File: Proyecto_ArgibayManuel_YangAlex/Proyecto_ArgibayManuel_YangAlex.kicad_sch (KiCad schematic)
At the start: 27 parts, among them J2 Conn_01x04, J3 Conn_01x06, J4 Conn_01x05, SW1 SW_Push, SW2 SW_Push, SW3 SW_Push, SW4 SW_Push, U1 PIC18F258-I_SO, U2 LT1716IS5TRMPBF, U3 LT1716IS5TRMPBF, U7 HDC2010YPAR, U8 TXS0108EPW, Y1 Crystal

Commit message: icsp
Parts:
- added J5: Conn_01x03_Pin, symbol Connector:Conn_01x03_Pin
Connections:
- net F_C_Out1: now also U1.17 (RC6/TX/CK); no longer U1.25 (RB4)
- net F_C_Out2: now also U1.18 (RC7/RX/DT); no longer U1.26 (RB5/PGM)
- net MCLR: now also J5.2 (Pin_2); no longer R3.1, SW4.1
- net PGC: now reaches U1.27 (RB6/PGC)
- net PGD: now reaches U1.28 (RB7/PGD)
- net +12V renamed VBat
- new net: J5.1 (Pin_1), R3.1, SW4.1
- new net PGM: U1.26 (RB5/PGM)
- new net Vpp: J5.3 (Pin_3)
- no-connect marks 26 -> 23
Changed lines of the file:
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@@
 	)
 	(junction
-		(at 33.02 27.94)
-		(diameter 0)
-		(color 0 0 0 0)
-	)
-	(junction
 		(at 250.19 39.37)
 		(diameter 0)
@@
 	)
 	(junction
-		(at 152.4 170.18)
+		(at 157.48 170.18)
 		(diameter 0)
 		(color 0 0 0 0)
@@
 	)
 	(no_connect
-		(at 110.49 125.73)
-	)
-	(no_connect
 		(at 247.65 59.69)
 	)
@@
 	)
 	(no_connect
-		(at 267.97 57.15)
+		(at 110.49 134.62)
 	)
 	(no_connect
-		(at 110.49 166.37)
+		(at 267.97 57.15)
 	)
 	(no_connect
@@
 	)
 	(no_connect
-		(at 110.49 129.54)
-	)
-	(no_connect
 		(at 267.97 54.61)
 	)
 	(no_connect
-		(at 110.49 163.83)
-	)
-	(no_connect
 		(at 267.97 67.31)
 	)
@@
 	(wire
 		(pts
-			(xy 30.48 27.94) (xy 33.02 27.94)
-		)
-		(stroke
-			(width 0)
-			(type default)
-		)
-	)
-	(wire
-		(pts
 			(xy 205.74 151.13) (xy 213.36 151.13)
 		)
@@
 	(wire
 		(pts
-			(xy 152.4 170.18) (xy 158.75 170.18)
+			(xy 152.4 170.18) (xy 157.48 170.18)
 		)
 		(stroke
@@
 	(wire
 		(pts
-			(xy 66.04 45.72) (xy 67.31 45.72)
+			(xy 157.48 170.18) (xy 157.48 180.34)
 		)
 		(stroke
@@
 	(wire
 		(pts
-			(xy 99.06 109.22) (xy 99.06 110.49)
+			(xy 66.04 45.72) (xy 67.31 45.72)
 		)
 		(stroke
@@
 	(wire
 		(pts
-			(xy 149.86 170.18) (xy 152.4 170.18)
+			(xy 99.06 109.22) (xy 99.06 110.49)
 		)
 		(stroke
@@
 	(wire
 		(pts
-			(xy 33.02 27.94) (xy 33.02 35.56)
-		)
-		(stroke
-			(width 0)
-			(type default)
-		)
-	)
-	(wire
-		(pts
 			(xy 250.19 39.37) (xy 250.19 43.18)
 		)
@@
 	(wire
 		(pts
-			(xy 33.02 26.67) (xy 33.02 27.94)
+			(xy 33.02 25.4) (xy 33.02 35.56)
 		)
 		(stroke
@@
 	(wire
 		(pts
+			(xy 157.48 180.34) (xy 152.4 180.34)
+		)
+		(stroke
+			(width 0)
+			(type default)
+		)
+	)
+	(wire
+		(pts
 			(xy 87.63 194.31) (xy 91.44 194.31)
 		)
@@
 	(wire
 		(pts
+			(xy 157.48 170.18) (xy 158.75 170.18)
+		)
+		(stroke
+			(width 0)
+			(type default)
+		)
+	)
+	(wire
+		(pts
 			(xy 238.76 39.37) (xy 240.03 39.37)
 		)
@@
 	(wire
 		(pts
+			(xy 152.4 182.88) (xy 157.48 182.88)
+		)
+		(stroke
+			(width 0)
+			(type default)
+		)
+	)
+	(wire
+		(pts
 			(xy 25.4 128.27) (xy 27.94 128.27)
 		)
@@
 	(wire
 		(pts
+			(xy 152.4 185.42) (xy 154.94 185.42)
+		)
+		(stroke
+			(width 0)
+			(type default)
+		)
+	)
+	(wire
+		(pts
 			(xy 48.26 35.56) (xy 41.91 35.56)
 		)
@@
 	(global_label "VBat"
 		(shape input)
-		(at 30.48 27.94 180)
+		(at 33.02 25.4 0)
 		(fields_autoplaced yes)
 		(effects
@@
 				(size 1.27 1.27)
 			)
-			(justify right)
+			(justify left)
 		)
 		(property "Intersheetrefs" "${INTERSHEET_REFS}"
-			(at 23.2615 27.94 0)
+			(at 40.2385 25.4 0)
 			(effects
 				(font
 					(size 1.27 1.27)
 				)
-				(justify right)
+				(justify left)
 				(hide yes)
 			)
@@
 	(global_label "F_C_Out2"
 		(shape input)
-		(at 110.49 132.08 0)
+		(at 110.49 163.83 0)
 		(fields_autoplaced yes)
 		(effects
@@
 		)
 		(property "Intersheetrefs" "${INTERSHEET_REFS}"
-			(at 122.1837 132.08 0)
+			(at 122.1837 163.83 0)
 			(effects
 				(font
@@
 	(global_label "MCLR"
 		(shape input)
-		(at 149.86 170.18 180)
+		(at 157.48 182.88 0)
 		(fields_autoplaced yes)
 		(effects
@@
 				(size 1.27 1.27)
 			)
-			(justify right)
+			(justify left)
 		)
 		(property "Intersheetrefs" "${INTERSHEET_REFS}"
-			(at 141.8553 170.18 0)
+			(at 165.4847 182.88 0)
 			(effects
 				(font
 					(size 1.27 1.27)
 				)
-				(justify right)
+				(justify left)
 				(hide yes)
 			)
@@
 		)
 	)
+	(global_label "PGM"
+		(shape input)
+		(at 110.49 132.08 0)
+		(fields_autoplaced yes)
+		(effects
+			(font
+				(size 1.27 1.27)
+			)
+			(justify left)
+		)
+		(property "Intersheetrefs" "${INTERSHEET_REFS}"
+			(at 117.4666 132.08 0)
+			(effects
+				(font
+					(size 1.27 1.27)
+				)
+				(justify left)
+				(hide yes)
+			)
+		)
+	)
 	(global_label "F_C_Out1"
 		(shape input)
-		(at 110.49 134.62 0)
+		(at 110.49 166.37 0)
 		(fields_autoplaced yes)
 		(effects
@@
 		)
 		(property "Intersheetrefs" "${INTERSHEET_REFS}"
-			(at 122.1837 134.62 0)
+			(at 122.1837 166.37 0)
 			(effects
 				(font
@@
 		)
 	)
+	(global_label "Vpp"
+		(shape input)
+		(at 154.94 185.42 0)
+		(fields_autoplaced yes)
+		(effects
+			(font
+				(size 1.27 1.27)
+			)
+			(justify left)
+		)
+		(property "Intersheetrefs" "${INTERSHEET_REFS}"
+			(at 161.3118 185.42 0)
+			(effects
+				(font
+					(size 1.27 1.27)
+				)
+				(justify left)
+				(hide yes)
+			)
+		)
+	)
+	(global_label "PGC"
+		(shape input)
+		(at 110.49 129.54 0)
+		(fields_autoplaced yes)
+		(effects
+			(font
+				(size 1.27 1.27)
+			)
+			(justify left)
+		)
+		(property "Intersheetrefs" "${INTERSHEET_REFS}"
+			(at 117.2852 129.54 0)
+			(effects
+				(font
+					(size 1.27 1.27)
+				)
+				(justify left)
+				(hide yes)
+			)
+		)
+	)
 	(global_label "C_R_Calefactor"
 		(shape input)
@@
 		)
 	)
+	(global_label "PGD"
+		(shape input)
+		(at 110.49 125.73 0)
+		(fields_autoplaced yes)
+		(effects
+			(font
+				(size 1.27 1.27)
+			)
+			(justify left)
+		)
+		(property "Intersheetrefs" "${INTERSHEET_REFS}"
+			(at 117.2852 125.73 0)
+			(effects
+				(font
+					(size 1.27 1.27)
+				)
+				(justify left)
+				(hide yes)
+			)
+		)
+	)
 	(global_label "TX1"
 		(shape input)
@@
 	)
 	(symbol
+		(lib_id "Connector:Conn_01x03_Pin")
+		(at 147.32 182.88 0)
+		(unit 1)
+		(exclude_from_sim no)
+		(in_bom yes)
+		(on_board yes)
+		(dnp no)
+		(fields_autoplaced yes)
+		(property "Reference" "J5"
+			(at 147.955 175.26 0)
+			(effects
+				(font
+					(size 1.27 1.27)
+				)
+			)
+		)
+		(property "Value" "Conn_01x03_Pin"
+			(at 147.955 177.8 0)
+			(effects
+				(font
+					(size 1.27 1.27)
+				)
+			)
+		)
+		(property "Footprint" ""
+			(at 147.32 182.88 0)
+			(effects
+				(font
+					(size 1.27 1.27)
+				)
+				(hide yes)
+			)
+		)
+		(property "Datasheet" "~"
+			(at 147.32 182.88 0)
+			(effects
+				(font
+					(size 1.27 1.27)
+				)
+				(hide yes)
+			)
+		)
+		(property "Description" "Generic connector, single row, 01x03, script generated"
+			(at 147.32 182.88 0)
+			(effects
+				(font
+					(size 1.27 1.27)
+				)
+				(hide yes)
+			)
+		)
+		(pin "3"
+		)
+		(pin "1"
+		)
+		(pin "2"
+		)
+		(instances
+			(project ""
+				(path "/b2dde924-33f5-41ab-a1bf-811873450a89"
+					(reference "J5")
+					(unit 1)
+				)
+			)
+		)
+	)
+	(symbol
 		(lib_id "Device:R")
 		(at 217.17 151.13 270)
@@
 					(unit 1)
 				)
-			)
-		)
-	)
-	(symbol
-		(lib_id "power:+12V")
-		(at 33.02 26.67 0)
-		(unit 1)
-		(exclude_from_sim no)
-		(in_bom yes)
-		(on_board yes)
-		(dnp no)
-		(property "Reference" "#PWR02"
-			(at 33.02 30.48 0)
-			(effects
-				(font
-					(size 1.27 1.27)
-				)
-				(hide yes)
-			)
-		)
-		(property "Value" "+12V"
-			(at 36.322 24.13 0)
-			(effects
-				(font
-					(size 1.27 1.27)
-				)
-			)
-		)
-		(property "Footprint" ""
-			(at 33.02 26.67 0)
-			(effects
-				(font
-					(size 1.27 1.27)
-				)
-				(hide yes)
-			)
-		)
-		(property "Datasheet" ""
-			(at 33.02 26.67 0)
-			(effects
-				(font
-					(size 1.27 1.27)
-				)
-				(hide yes)
-			)
-		)
-		(property "Description" "Power symbol creates a global label with name \"+12V\""
-			(at 33.02 26.67 0)
-			(effects
-				(font
-					(size 1.27 1.27)
-				)
-				(hide yes)
-			)
-		)
-		(pin "1"
-		)
-		(instances
-			(project ""
-				(path "/b2dde924-33f5-41ab-a1bf-811873450a89"
-					(reference "#PWR02")
-					(unit 1)
-				)

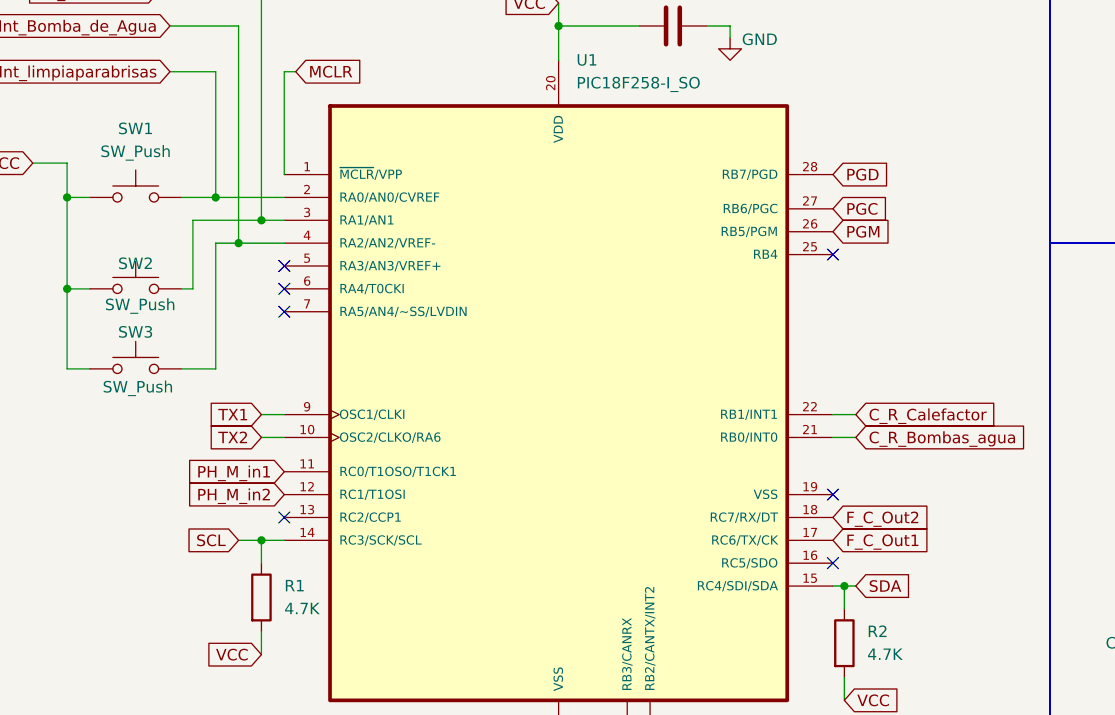
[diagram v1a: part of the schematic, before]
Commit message: Arreglo net classes, agrego DB-9
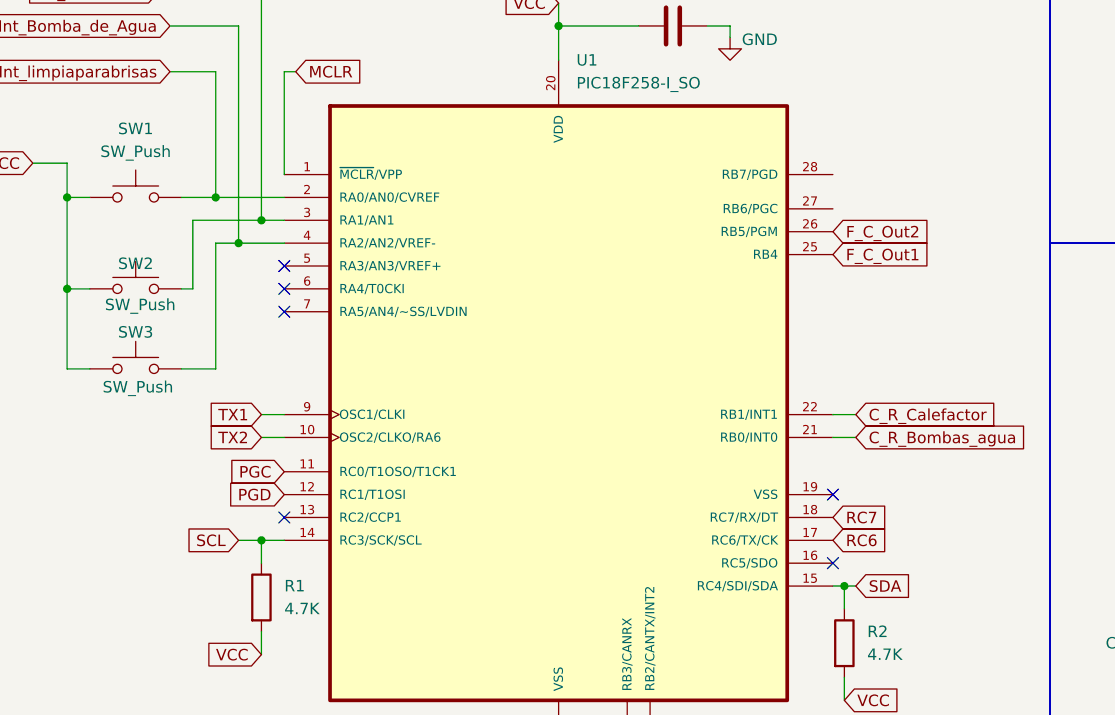
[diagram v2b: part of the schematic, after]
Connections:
- net PGM is gone; now on net F_C_Out2: U1.26 (RB5/PGM)
- net PH_M_in1 is gone; now on net PGC: U1.11 (RC0/T1OSO/T1CK1)
- net PH_M_in2 is gone; now on net PGD: U1.12 (RC1/T1OSI)
- net F_C_Out1: now also U1.25 (RB4); no longer U1.17 (RC6/TX/CK)
- net F_C_Out2: no longer U1.18 (RC7/RX/DT)
- net PGC: no longer U1.27 (RB6/PGC)
- net PGD: no longer U1.28 (RB7/PGD)
- new net RC6: U1.17 (RC6/TX/CK)
- new net RC7: U1.18 (RC7/RX/DT)
- no-connect marks 23 -> 22

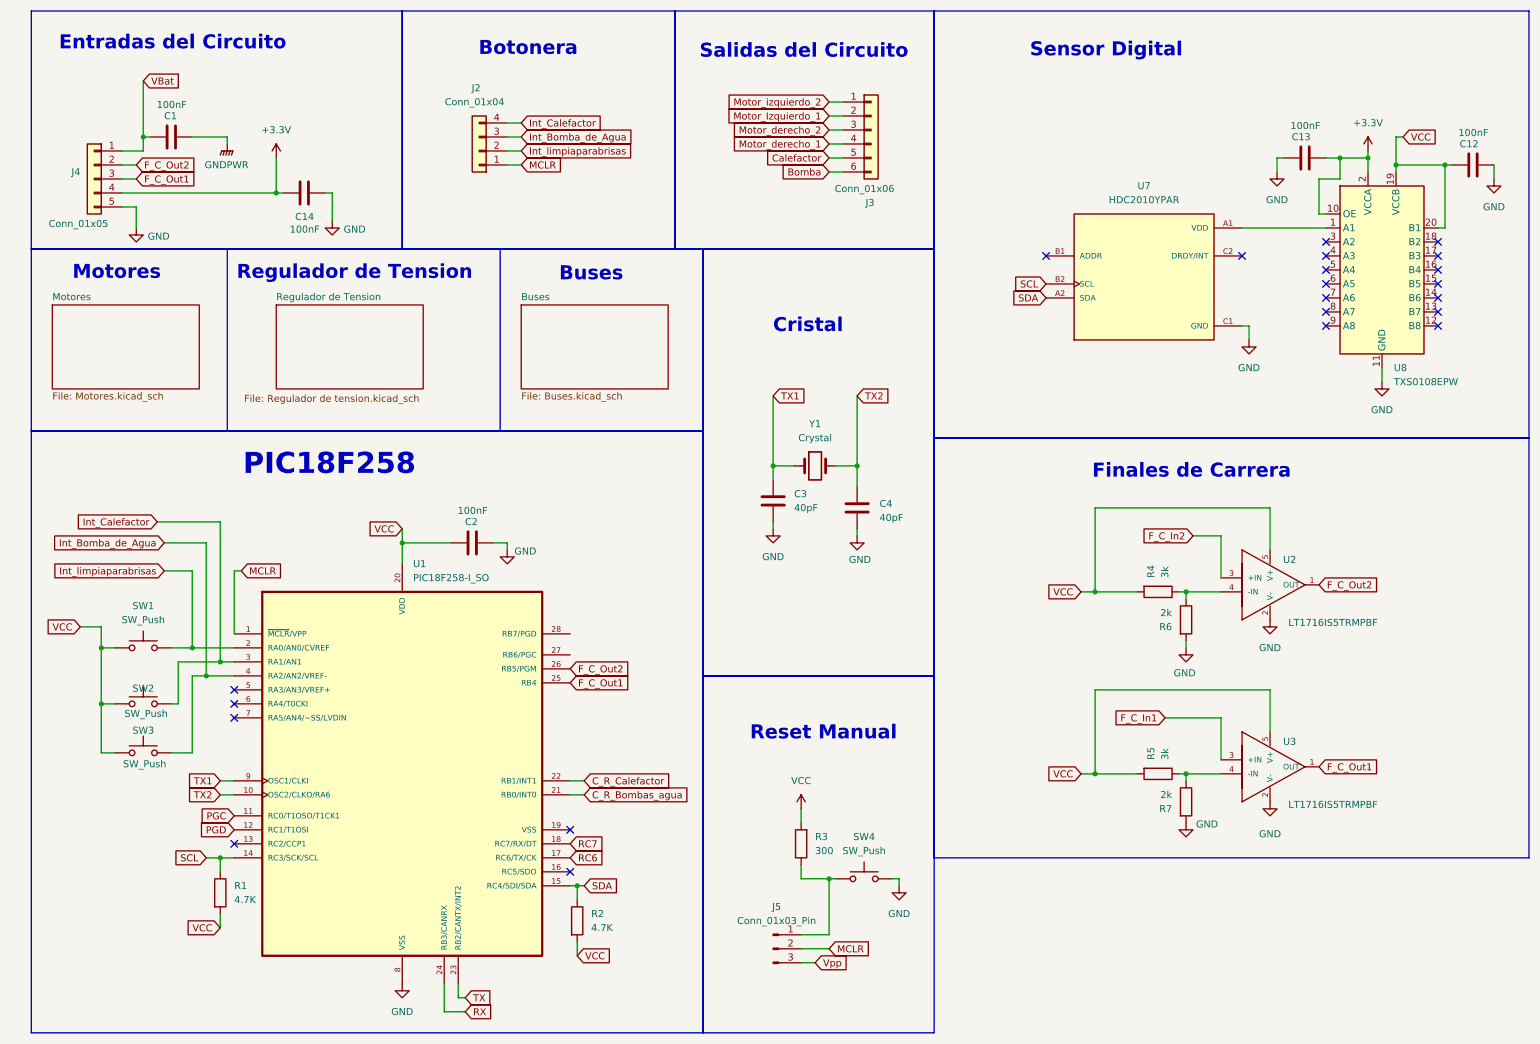
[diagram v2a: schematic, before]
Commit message: Empiezo layout, cambio footprints y arreglo esquematico
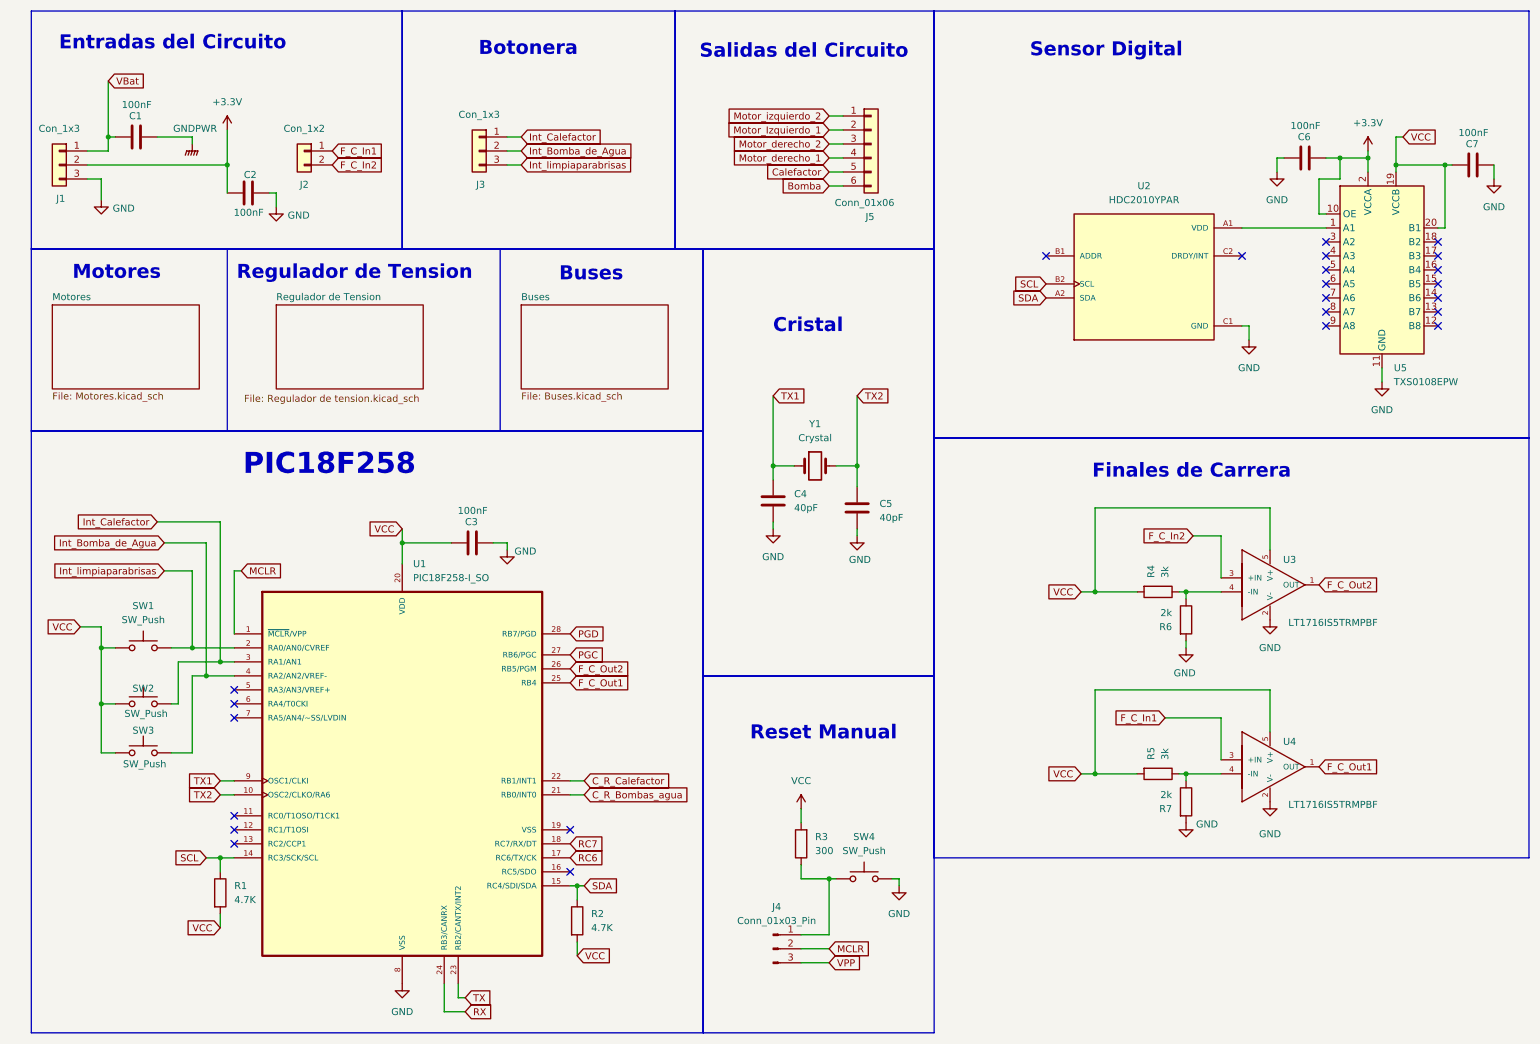
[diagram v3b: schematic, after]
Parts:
- removed J2: Conn_01x04, Connector_PinHeader_2.54mm:PinHeader_1x04_P2.54mm_Vertical, symbol Connector_Generic:Conn_01x04
- removed J4: Conn_01x05, Connector_PinHeader_2.54mm:PinHeader_1x04_P2.54mm_Vertical, symbol Connector_Generic:Conn_01x05
- added J1, J3: Con_1x3, Connector_PinHeader_2.54mm:PinHeader_1x03_P2.54mm_Vertical, symbol Connector_Generic:Conn_01x03
- added J2: Con_1x2, Connector_PinHeader_2.54mm:PinHeader_1x02_P2.54mm_Vertical, symbol Connector_Generic:Conn_01x02
- C1: footprint Capacitor_SMD:C_0805_2012Metric -> Capacitor_THT:CP_Radial_D5.0mm_P2.00mm
- C2: renamed from C14; footprint Capacitor_SMD:C_0805_2012Metric -> Capacitor_THT:CP_Radial_D5.0mm_P2.00mm
- C3: renamed from C2; footprint Capacitor_SMD:C_0805_2012Metric -> Capacitor_THT:CP_Radial_D5.0mm_P2.00mm
- C6: renamed from C13; footprint Capacitor_SMD:C_0805_2012Metric -> Capacitor_THT:CP_Radial_D5.0mm_P2.00mm
- C7: renamed from C12; footprint Capacitor_SMD:C_0805_2012Metric -> Capacitor_THT:CP_Radial_D5.0mm_P2.00mm
- J4: renamed from J5; footprint (none) -> Connector_PinHeader_2.54mm:PinHeader_1x03_P2.54mm_Vertical
- R1, R2, R3, R4, R5, R6, R7: footprint Resistor_THT:R_Axial_DIN0204_L3.6mm_D1.6mm_P1.90mm_Vertical -> Resistor_SMD:R_0805_2012Metric
- U1: footprint PIC18F258-I_SO:SOIC127P1030X265-28N -> Footprints:PIC18F258
- U2: renamed from U7; footprint HDC2010YPAR:BGA6C100X50P2X3_HDC2010YPAR -> Footprints:HDC2010YPAR
- U3: renamed from U2; footprint LT1716IS5TRMPBF:SOT-5_S -> Footprints:LT1716
- U4: renamed from U3; footprint LT1716IS5TRMPBF:SOT-5_S -> Footprints:LT1716
- renumbered C3 to C4, C4 to C5, J3 to J5, U8 to U5
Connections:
- net +3.3V: now also J1.2 (Pin_2)
- net F_C_In1: now also J2.1 (Pin_1)
- net F_C_In2: now also J2.2 (Pin_2)
- net GND: now also J1.3 (Pin_3)
- net Int_Bomba_de_Agua: now also J3.2 (Pin_2)
- net Int_Calefactor: now also J3.1 (Pin_1)
- net Int_limpiaparabrisas: now also J3.3 (Pin_3)
- net PGC: now also U1.27 (RB6/PGC); no longer U1.11 (RC0/T1OSO/T1CK1)
- net PGD: now also U1.28 (RB7/PGD); no longer U1.12 (RC1/T1OSI)
- net VBat: now also J1.1 (Pin_1)
- net Vpp renamed VPP
- no-connect marks 22 -> 24
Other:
- moved on the sheet: C1, C2, J5
